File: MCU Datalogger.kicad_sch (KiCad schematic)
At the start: 25 parts, among them U1 24LC1025, U2 DS1337S_, U3 24LC1025, U4 ATMEGA328P-AU, Y1 32.768 MHz, Y2 16 MHz

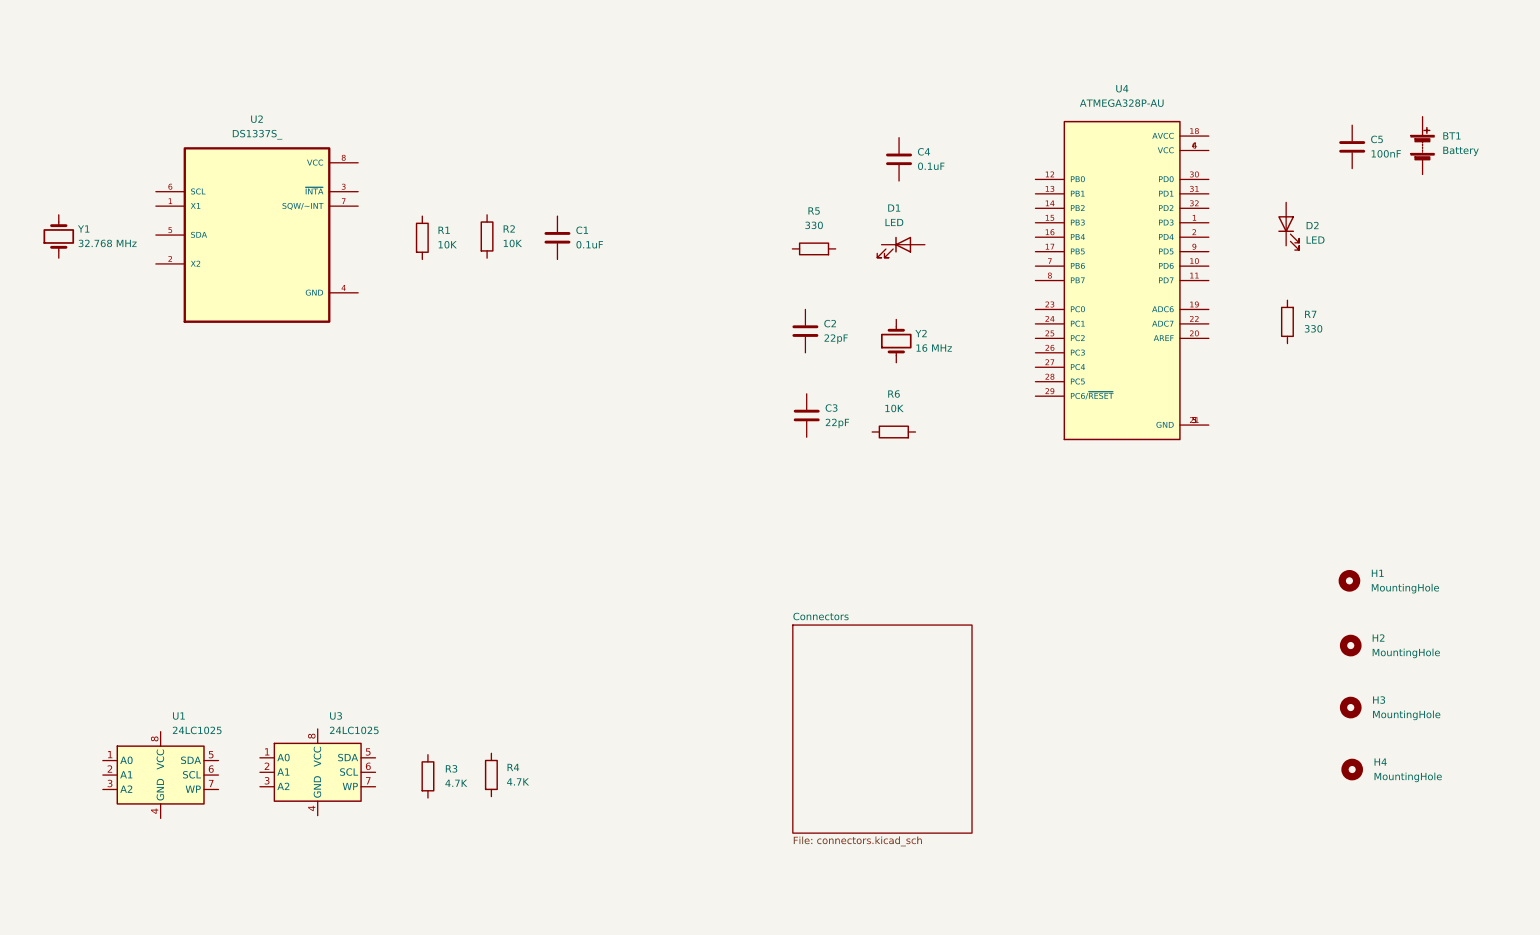
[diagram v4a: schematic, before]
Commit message: Completed wiring of main sheet.
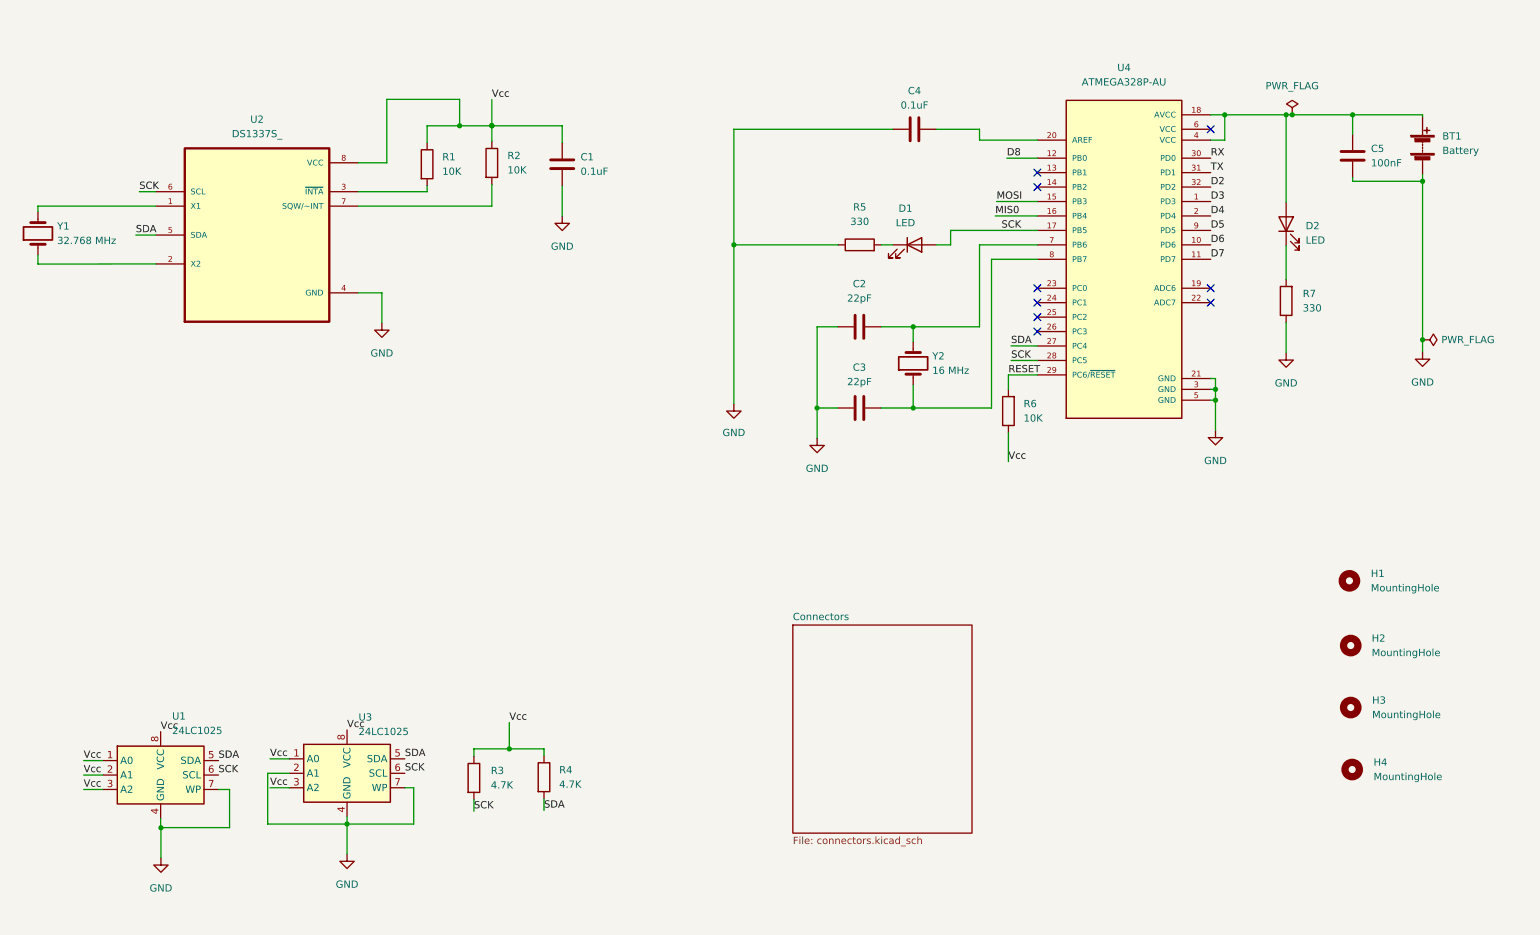
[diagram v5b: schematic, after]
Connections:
- net at C5.1: now also BT1.1 (+), D2.2 (A), U4.18 (AVCC), U4.4 (VCC)
- net GND: now reaches C5.2
- net GND: now also BT1.2 (-), C1.2, C2.2, C3.1, C4.1, R5.1, R7.1, U2.4 (GND), U3.2 (A1), U3.4 (GND), U3.7 (WP), U4.21 (GND), U4.3 (GND), U4.5 (GND)
- net Vcc: now reaches R4.1
- net Vcc: now also R3.1, R6.1, U1.1 (A0), U1.2 (A1), U1.3 (A2), U1.8 (VCC), U3.1 (A0), U3.3 (A2), U3.8 (VCC)
- net SDA: now reaches R4.2
- net SDA: now also U1.5 (SDA), U2.5 (SDA), U3.5 (SDA), U4.27 (PC4)
- net at U2.1 (X1): now also Y1.2
- net at U2.2 (X2): now also Y1.1
- net at U2.3 (~{INTA}): now also R1.2
- net SCK: now reaches U2.6 (SCL)
- net SCK: now also D1.2 (A), R3.2, U1.6 (SCL), U3.6 (SCL), U4.17 (PB5), U4.28 (PC5)
- net at U2.7 (SQW/~INT): now also R2.2
- net at U2.8 (VCC): now also C1.1, R1.1, R2.1
- net at R5.2: now also D1.1 (K)
- net at C2.1: now also U4.7 (PB6), Y2.2
- net at R7.2: now also D2.1 (K)
- net at C4.2: now also U4.20 (AREF)
- net at C3.2: now also U4.8 (PB7), Y2.1
- net at U1.4 (GND): now also U1.7 (WP)
- net RESET: now reaches R6.2
- net RESET: now also U4.29 (PC6/~{RESET})
- net D3: now reaches U4.1 (PD3)
- net D6: now reaches U4.10 (PD6)
- net D7: now reaches U4.11 (PD7)
- net D8: now reaches U4.12 (PB0)
- net MOSI: now reaches U4.15 (PB3)
- net MIS0: now reaches U4.16 (PB4)
- net D4: now reaches U4.2 (PD4)
- net RX: now reaches U4.30 (PD0)
- net TX: now reaches U4.31 (PD1)
- net D2: now reaches U4.32 (PD2)
- net at U4.6 (VCC): no longer U4.4 (VCC)
- net D5: now reaches U4.9 (PD5)
- no-connect marks 0 -> 9
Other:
- moved on the sheet: C1, C2, C3, C4, C5, D1, R1, R2, R3, R4, R5, R6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

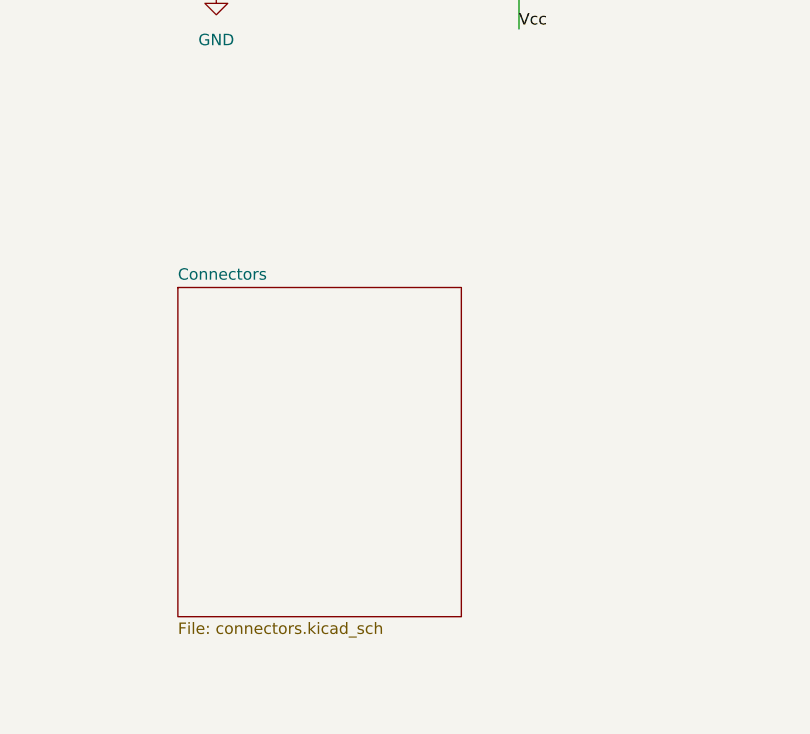
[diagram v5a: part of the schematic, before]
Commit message: Allocated GND and Vcc nets to the Power net
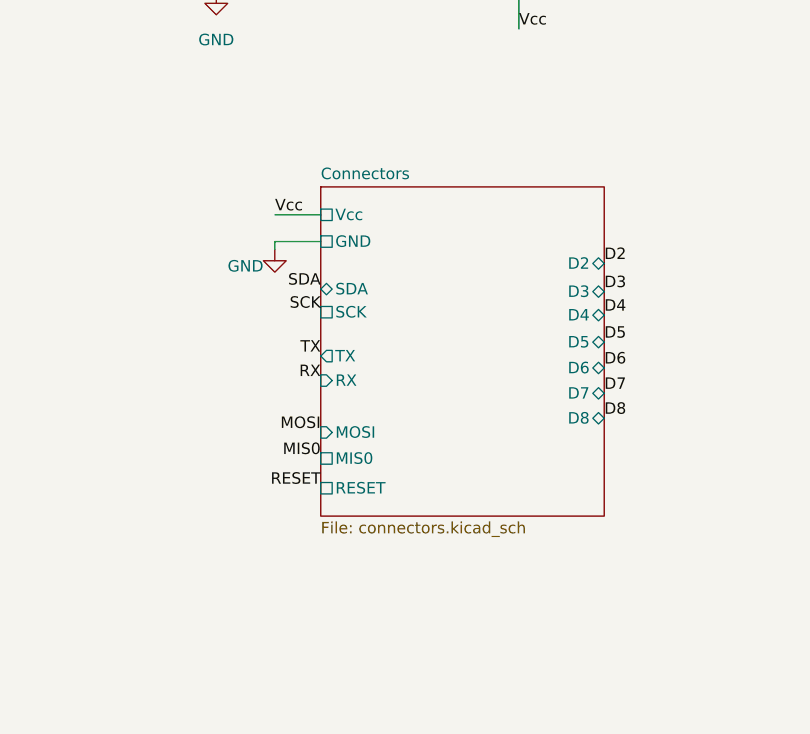
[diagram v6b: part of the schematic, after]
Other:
- sheet Connectors ports: added D2, D3, D4, D5, D6, D7, D8, GND, MIS0, MOSI, RESET, RX, SCK, SDA, TX, Vcc; removed none
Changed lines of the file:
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@@
+    (stroke (width 0) (type default) (color 0 0 0 0))
+  )
+  (wire (pts (xy 168.4782 117.602) (xy 163.3728 117.602))
     (stroke (width 0) (type default) (color 0 0 0 0))
   )
@@
     (stroke (width 0) (type default) (color 0 0 0 0))
   )
+  (wire (pts (xy 163.3728 117.602) (xy 163.3728 118.4656))
+    (stroke (width 0) (type default) (color 0 0 0 0))
+  )
   (wire (pts (xy 263.2964 43.5102) (xy 263.2964 44.704))
     (stroke (width 0) (type default) (color 0 0 0 0))
@@
     (stroke (width 0) (type default) (color 0 0 0 0))
   )
+  (wire (pts (xy 163.3982 114.6302) (xy 168.4782 114.6302))
+    (stroke (width 0) (type default) (color 0 0 0 0))
+  )
   (wire (pts (xy 142.24 55.88) (xy 142.24 83.82))
     (stroke (width 0) (type default) (color 0 0 0 0))
@@
     (effects (font (size 1.27 1.27)) (justify left bottom))
   )
+  (label "D2" (at 199.9742 120.0404 0)
+    (effects (font (size 1.27 1.27)) (justify left bottom))
+  )
   (label "D2" (at 226.06 45.72 0)
     (effects (font (size 1.27 1.27)) (justify left bottom))
@@
     (effects (font (size 1.27 1.27)) (justify left bottom))
   )
+  (label "RX" (at 168.4782 133.0452 180)
+    (effects (font (size 1.27 1.27)) (justify right bottom))
+  )
   (label "D5" (at 226.06 53.34 0)
     (effects (font (size 1.27 1.27)) (justify left bottom))
@@
     (effects (font (size 1.27 1.27)) (justify left bottom))
   )
+  (label "TX" (at 168.4782 130.3274 180)
+    (effects (font (size 1.27 1.27)) (justify right bottom))
+  )
+  (label "SDA" (at 168.4782 122.8852 180)
+    (effects (font (size 1.27 1.27)) (justify right bottom))
+  )
   (label "D4" (at 226.06 50.8 0)
     (effects (font (size 1.27 1.27)) (justify left bottom))
@@
     (effects (font (size 1.27 1.27)) (justify left bottom))
   )
+  (label "D8" (at 199.9742 137.2362 0)
+    (effects (font (size 1.27 1.27)) (justify left bottom))
+  )
+  (label "D7" (at 199.9742 134.4676 0)
+    (effects (font (size 1.27 1.27)) (justify left bottom))
+  )
   (label "RX" (at 226.06 40.64 0)
     (effects (font (size 1.27 1.27)) (justify left bottom))
   )
+  (label "D5" (at 199.9742 128.778 0)
+    (effects (font (size 1.27 1.27)) (justify left bottom))
+  )
   (label "SCK" (at 51.6382 149.0726 0)
     (effects (font (size 1.27 1.27)) (justify left bottom))
   )
+  (label "D3" (at 199.9742 123.1646 0)
+    (effects (font (size 1.27 1.27)) (justify left bottom))
+  )
   (label "SDA" (at 190.9572 73.6346 0)
     (effects (font (size 1.27 1.27)) (justify left bottom))
@@
     (effects (font (size 1.27 1.27)) (justify left bottom))
   )
+  (label "D4" (at 199.9742 125.7808 0)
+    (effects (font (size 1.27 1.27)) (justify left bottom))
+  )
+  (label "D6" (at 199.9742 131.6482 0)
+    (effects (font (size 1.27 1.27)) (justify left bottom))
+  )
   (label "SDA" (at 51.6382 146.5326 0)
     (effects (font (size 1.27 1.27)) (justify left bottom))
@@
     (effects (font (size 1.27 1.27)) (justify left bottom))
   )
+  (label "Vcc" (at 163.3982 114.6302 0)
+    (effects (font (size 1.27 1.27)) (justify left bottom))
+  )
   (label "Vcc" (at 27.94 151.6126 0)
     (effects (font (size 1.27 1.27)) (justify left bottom))
   )
+  (label "SCK" (at 168.4782 125.4506 180)
+    (effects (font (size 1.27 1.27)) (justify right bottom))
+  )
   (label "Vcc" (at 60.706 146.2278 0)
     (effects (font (size 1.27 1.27)) (justify left bottom))
@@
     (effects (font (size 1.27 1.27)) (justify left bottom))
   )
+  (label "MOSI" (at 168.4782 138.811 180)
+    (effects (font (size 1.27 1.27)) (justify right bottom))
+  )
+  (label "RESET" (at 168.4782 145.0086 180)
+    (effects (font (size 1.27 1.27)) (justify right bottom))
+  )
   (label "D3" (at 226.06 48.26 0)
     (effects (font (size 1.27 1.27)) (justify left bottom))
+  )
+  (label "MIS0" (at 168.4782 141.7066 180)
+    (effects (font (size 1.27 1.27)) (justify right bottom))
   )
   (label "SCK" (at 84.4042 148.7678 0)
@@
     (pin "7")
     (pin "8")
+  )
+  (symbol (lib_id "power:GND") (at 163.3728 118.4656 0) (unit 1)
+    (in_bom yes) (on_board yes)
+    (property "Reference" "#PWR?" (id 0) (at 163.3728 124.8156 0)
+      (effects (font (size 1.27 1.27)) hide)
+    )
+    (property "Value" "GND" (id 1) (at 160.1216 120.3452 0))
+    (property "Footprint" "" (id 2) (at 163.3728 118.4656 0)
+      (effects (font (size 1.27 1.27)) hide)
+    )
+    (property "Datasheet" "" (id 3) (at 163.3728 118.4656 0)
+      (effects (font (size 1.27 1.27)) hide)
+    )
+    (pin "1")
   )
   (symbol (lib_id "power:GND") (at 112.0648 50.8254 0) (unit 1)
@@
     (pin "2")
   )
-  (sheet (at 152.6032 122.7074) (size 31.496 36.576) (fields_autoplaced)
+  (sheet (at 168.4782 111.5314) (size 31.496 36.576) (fields_autoplaced)
     (stroke (width 0.1524) (type solid) (color 0 0 0 0))
     (fill (color 0 0 0 0.0000))
-    (property "Sheet name" "Connectors" (id 0) (at 152.6032 121.9958 0)
+    (property "Sheet name" "Connectors" (id 0) (at 168.4782 110.8198 0)
       (effects (font (size 1.27 1.27)) (justify left bottom))
     )
-    (property "Sheet file" "connectors.kicad_sch" (id 1) (at 152.6032 159.868 0)
+    (property "Sheet file" "connectors.kicad_sch" (id 1) (at 168.4782 148.692 0)
       (effects (font (size 1.27 1.27)) (justify left top))
+    )
+    (pin "Vcc" passive (at 168.4782 114.6302 180)
+      (effects (font (size 1.27 1.27)) (justify left))
+    )
+    (pin "MOSI" input (at 168.4782 138.811 180)
+      (effects (font (size 1.27 1.27)) (justify left))
+    )
+    (pin "GND" passive (at 168.4782 117.602 180)
+      (effects (font (size 1.27 1.27)) (justify left))
+    )
+    (pin "SCK" passive (at 168.4782 125.4506 180)
+      (effects (font (size 1.27 1.27)) (justify left))
+    )
+    (pin "RESET" passive (at 168.4782 145.0086 180)
+      (effects (font (size 1.27 1.27)) (justify left))
+    )
+    (pin "MIS0" passive (at 168.4782 141.7066 180)
+      (effects (font (size 1.27 1.27)) (justify left))
+    )
+    (pin "D2" bidirectional (at 199.9742 120.0404 0)
+      (effects (font (size 1.27 1.27)) (justify right))
+    )
+    (pin "D3" bidirectional (at 199.9742 123.1646 0)
+      (effects (font (size 1.27 1.27)) (justify right))
+    )
+    (pin "D4" bidirectional (at 199.9742 125.7808 0)
+      (effects (font (size 1.27 1.27)) (justify right))
+    )
+    (pin "D5" bidirectional (at 199.9742 128.778 0)
+      (effects (font (size 1.27 1.27)) (justify right))
+    )
+    (pin "SDA" bidirectional (at 168.4782 122.8852 180)
+      (effects (font (size 1.27 1.27)) (justify left))
+    )
+    (pin "D6" bidirectional (at 199.9742 131.6482 0)
+      (effects (font (size 1.27 1.27)) (justify right))
+    )
+    (pin "D7" bidirectional (at 199.9742 134.4676 0)
+      (effects (font (size 1.27 1.27)) (justify right))
+    )
+    (pin "D8" bidirectional (at 199.9742 137.2362 0)
+      (effects (font (size 1.27 1.27)) (justify right))
+    )
+    (pin "RX" input (at 168.4782 133.0452 180)
+      (effects (font (size 1.27 1.27)) (justify left))
+    )
+    (pin "TX" output (at 168.4782 130.3274 180)
+      (effects (font (size 1.27 1.27)) (justify left))
     )
   )
@@
       (reference "#PWR?") (unit 1) (value "GND") (footprint "")
     )
+    (path "/dfa1bfd1-8a12-4bb1-8586-1dcc1c06a2f7"
+      (reference "#PWR?") (unit 1) (value "GND") (footprint "")
+    )

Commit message: Completed comments.
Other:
- note added: "EEPROM"
- note added: "MCU"
- note added: "Mounting"
- note added: "Real time clock"
